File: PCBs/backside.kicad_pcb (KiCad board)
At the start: 2 copper layers, 147.3 x 110.5 mm, 66 parts, among them J1 9Pin, J14 Conn_01x07_Male, J15 Conn_01x07_Male, J16 Conn_01x07_Male, J17 Conn_01x04_Male, J18 Conn_02x17_Odd_Even, J3 Power, J4 Conn_01x17_Male, J5 Matrix, J6 Conn_01x17_Male, J7 Driver output 2, J8 Conn_01x04_Male, J9 Conn_01x30_Male, U1 HT1632C-52LQFP, U2 HT1632C-52LQFP, U3 STM32F103C8T6

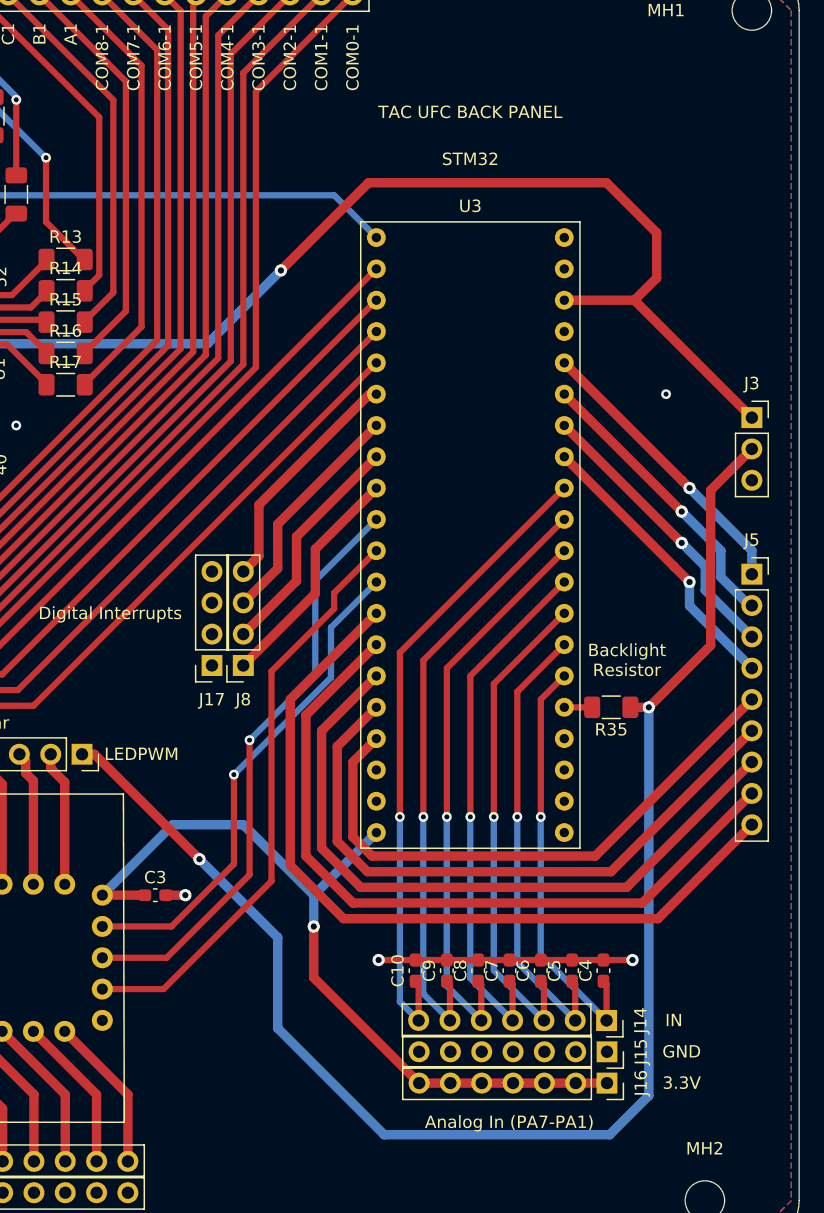
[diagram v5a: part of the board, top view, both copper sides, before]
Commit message: Fixed design error
Untested as of now.
Removed direct connection from PWM out to LEDs, as the PWM pins on the bluepill can't provide enough current. Added P channel mosfet, and individual resistors per parallel LED. For now, the single resistor for all LEDs is still present, but bypassable via jumper, for the sake of backwards compatibility.
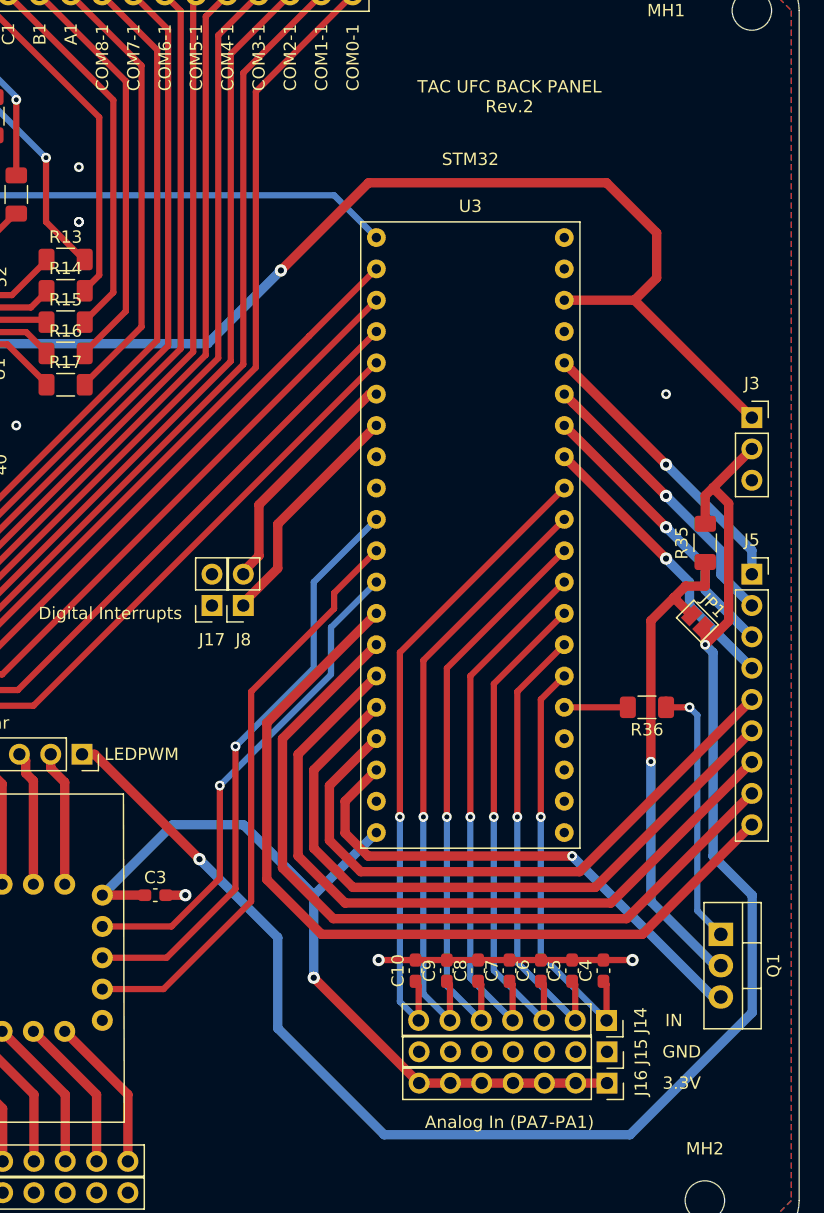
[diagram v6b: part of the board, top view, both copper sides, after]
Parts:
- added JP1: R35 Bypass, Jumper:SolderJumper-2_P1.3mm_Open_Pad1.0x1.5mm, F.Cu at (120.7, 101.6)
- added Q1: IPP120P04P4L03, Package_TO_SOT_THT:TO-220-3_Vertical, F.Cu at (122.6, 127.0)
- added R36: 100R, Resistor_SMD:R_1206_3216Metric_Pad1.30x1.75mm_HandSolder, F.Cu at (116.6, 108.6)
- J17, J8: value Conn_01x04_Male -> Conn_01x02_Male; footprint Connector_PinSocket_2.54mm:PinSocket_1x04_P2.54mm_Vertical -> Connector_PinSocket_2.54mm:PinSocket_1x02_P2.54mm_Vertical
- R35: value 100R -> 20R
- moved R35 15.4 mm to (121.3, 95.2), turned to 270 degrees
- moved J17 4.86 mm to (81.3, 100.3)
- moved J8 4.86 mm to (83.8, 100.3)
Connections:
- R35 pad 2: Net-(R35-Pad2) -> Net-(JP1-Pad1)
- U3 pad 10: Net-(R35-Pad2) -> Net-(R36-Pad2)
- U3 pad 30: /DigInt4 -> /DigInt2
- U3 pad 31: /DigInt3 -> /DigInt1
- U3 pad 32: /DigInt2 -> Net-(U3-Pad32)
- U3 pad 33: /DigInt1 -> Net-(U3-Pad33)
- U3 pad 50: Net-(U3-Pad50) -> /5V
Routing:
- net /5V: track 0.00 -> 42.2 mm, vias 0 -> 1
- net Net-(JP1-Pad1): track 0.00 -> 40.2 mm, vias 0 -> 1
- net Net-(Q1-Pad1): track 0.00 -> 22.0 mm, vias 0 -> 1
- net /DigInt4: track 19.2 -> 0.00 mm
- net /DigInt3: track 18.9 -> 0.00 mm
- net /LEDPWM: track 121.9 -> 130.2 mm
- net Net-(R36-Pad2): track 0.00 -> 5.16 mm
- net /ROW4: track 65.7 -> 70.1 mm
- net /ROW3: track 60.9 -> 65.2 mm
- net /ROW2: track 56.2 -> 60.4 mm
- net /ROW1: track 51.6 -> 55.6 mm
- net /ROW0: track 47.0 -> 50.9 mm
- net Net-(R35-Pad2): track 2.35 -> 0.00 mm
- net /GND: vias 15 -> 18
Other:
- board text added: "TAC UFC BACK PANEL Rev.2"
- board text removed: "Backlight Resistor"
- board text removed: "TAC UFC BACK PANEL"

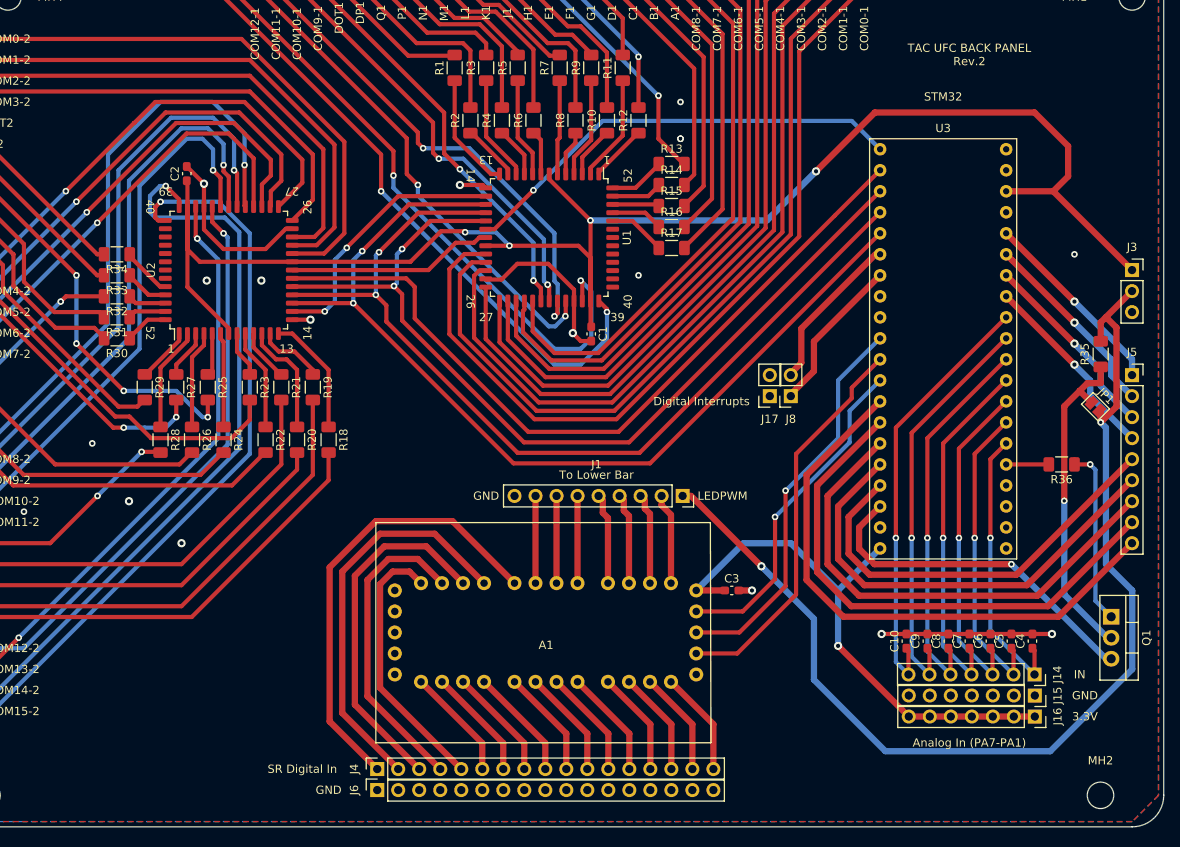
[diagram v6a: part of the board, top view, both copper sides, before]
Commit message: Major revision to backside PCB
Re-arranged pin assignments on the bluepill; sacrificed 4 Analog inputs for 2 more digital interrupts, and 2 more SPI CS pins.
Added two RJ12 connectors so that the board can be connected to other devices that use just shift registers, such as MFDs
Replaced footprint for 3x shift register sub-assembly PCB with 2 DIP16 74hc165s, and pullups and bypass caps.
Re-arranged and replaced 0.1" headers as appropriate.
Removed R35 and its bypass jumper, connecting LEDPWM directly to the MOSFET drain.
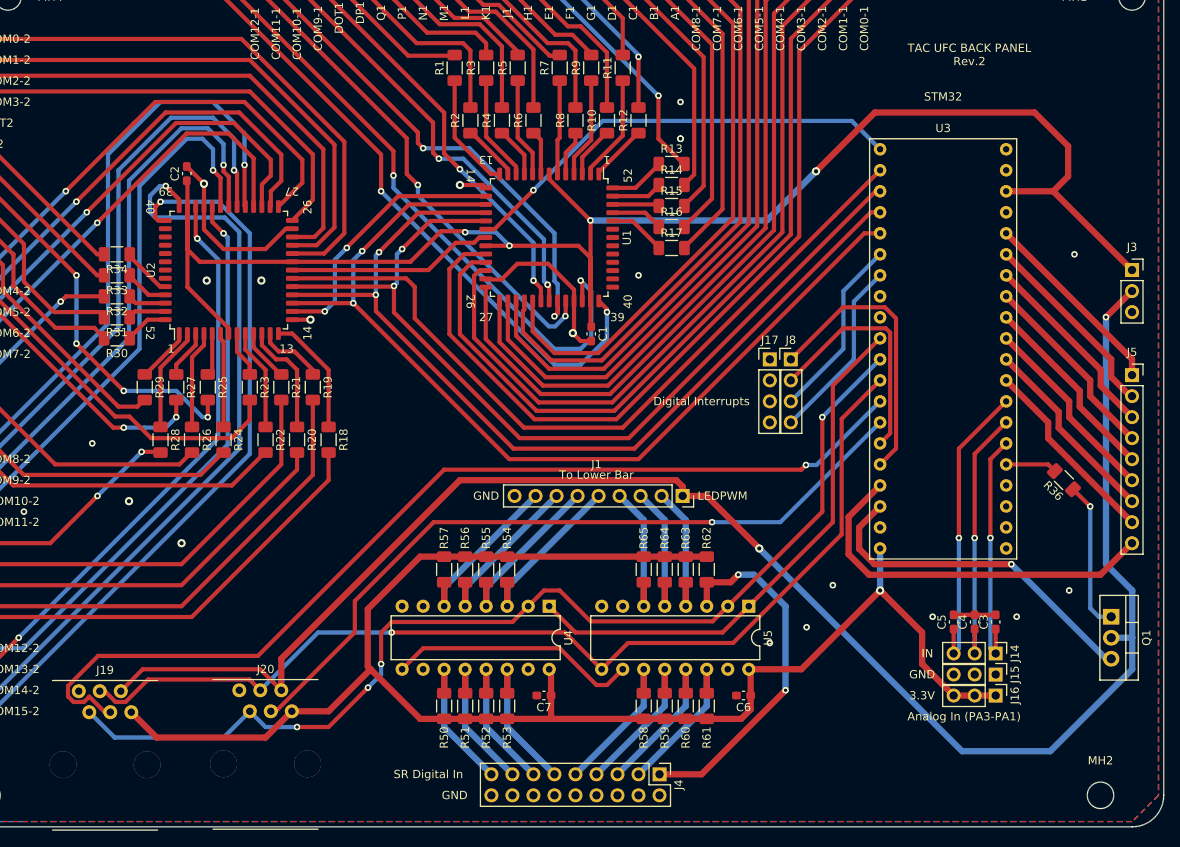
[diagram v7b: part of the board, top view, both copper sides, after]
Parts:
- removed A1: ShiftRegisterBoard, UFC:ShiftRegisterBoardPins
- removed C10, C8, C9: .1uF, Capacitor_SMD:C_0603_1608Metric_Pad1.08x0.95mm_HandSolder
- removed J6: Conn_01x17_Male, Connector_PinSocket_2.54mm:PinSocket_1x17_P2.54mm_Vertical
- removed JP1: R35 Bypass, Jumper:SolderJumper-2_P1.3mm_Open_Pad1.0x1.5mm
- removed R35: 20R, Resistor_SMD:R_1206_3216Metric_Pad1.30x1.75mm_HandSolder
- added J19: RJ12, UFC:SS-6466-NF, F.Cu at (0.91, 136.0)
- added J20: RJ12, UFC:SS-6466-NF, F.Cu at (20.3, 135.9)
- added R50: 10K, Resistor_SMD:R_1206_3216Metric_Pad1.30x1.75mm_HandSolder, F.Cu at (41.9, 137.8)
- added R51: 10K, Resistor_SMD:R_1206_3216Metric_Pad1.30x1.75mm_HandSolder, F.Cu at (44.5, 137.8)
- added R52: 10K, Resistor_SMD:R_1206_3216Metric_Pad1.30x1.75mm_HandSolder, F.Cu at (47.0, 137.8)
- added R53: 10K, Resistor_SMD:R_1206_3216Metric_Pad1.30x1.75mm_HandSolder, F.Cu at (49.5, 137.8)
- added R54: 10K, Resistor_SMD:R_1206_3216Metric_Pad1.30x1.75mm_HandSolder, F.Cu at (49.5, 121.3)
- added R55: 10K, Resistor_SMD:R_1206_3216Metric_Pad1.30x1.75mm_HandSolder, F.Cu at (47.0, 121.3)
- added R56: 10K, Resistor_SMD:R_1206_3216Metric_Pad1.30x1.75mm_HandSolder, F.Cu at (44.5, 121.3)
- added R57: 10K, Resistor_SMD:R_1206_3216Metric_Pad1.30x1.75mm_HandSolder, F.Cu at (41.9, 121.3)
- added R58: 10K, Resistor_SMD:R_1206_3216Metric_Pad1.30x1.75mm_HandSolder, F.Cu at (66.0, 137.8)
- added R59: 10K, Resistor_SMD:R_1206_3216Metric_Pad1.30x1.75mm_HandSolder, F.Cu at (68.6, 137.8)
- added R60: 10K, Resistor_SMD:R_1206_3216Metric_Pad1.30x1.75mm_HandSolder, F.Cu at (71.1, 137.8)
- added R61: 10K, Resistor_SMD:R_1206_3216Metric_Pad1.30x1.75mm_HandSolder, F.Cu at (73.7, 137.8)
- added R62: 10K, Resistor_SMD:R_1206_3216Metric_Pad1.30x1.75mm_HandSolder, F.Cu at (73.7, 121.3)
- added R63: 10K, Resistor_SMD:R_1206_3216Metric_Pad1.30x1.75mm_HandSolder, F.Cu at (71.1, 121.3)
- added R64: 10K, Resistor_SMD:R_1206_3216Metric_Pad1.30x1.75mm_HandSolder, F.Cu at (68.6, 121.3)
- added R65: 10K, Resistor_SMD:R_1206_3216Metric_Pad1.30x1.75mm_HandSolder, F.Cu at (66.0, 121.3)
- added U4: 74HC165, Package_DIP:DIP-16_W7.62mm, F.Cu at (54.6, 125.7)
- added U5: 74HC165, Package_DIP:DIP-16_W7.62mm, F.Cu at (78.7, 125.7)
- J14, J15, J16: value Conn_01x07_Male -> Conn_01x03_Male; footprint Connector_PinSocket_2.54mm:PinSocket_1x07_P2.54mm_Vertical -> Connector_PinHeader_2.54mm:PinHeader_1x03_P2.54mm_Vertical
- J17, J8: value Conn_01x02_Male -> Conn_01x04_Male; footprint Connector_PinSocket_2.54mm:PinSocket_1x02_P2.54mm_Vertical -> Connector_PinHeader_2.54mm:PinHeader_1x04_P2.54mm_Vertical
- J4: value Conn_01x17_Male -> Conn_02x09_Odd_Even; footprint Connector_PinSocket_2.54mm:PinSocket_1x17_P2.54mm_Vertical -> Connector_PinHeader_2.54mm:PinHeader_2x09_P2.54mm_Vertical
- moved C7 51.9 mm to (54.0, 136.5), turned to 180 degrees
- moved J4 34.1 mm to (67.9, 146.1), turned to 270 degrees
- moved C3 32.1 mm to (108.6, 127.6), turned to 90 degrees
- moved C6 30.6 mm to (78.1, 136.5), turned to 180 degrees
- moved C4 7.36 mm to (106.0, 127.6)
- moved C5 7.36 mm to (103.5, 127.6)
- moved J15 5.37 mm to (108.6, 134.0)
- moved J16 5.37 mm to (108.6, 136.5)
- moved J14 5.34 mm to (108.6, 131.4)
- moved J17 4.44 mm to (81.3, 95.9), turned to 0 degrees
- moved J8 4.44 mm to (83.8, 95.9), turned to 0 degrees
- moved R36 1.93 mm to (116.8, 110.5), turned to 135 degrees
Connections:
- C3 pad 1: /3.3V -> /Analog1
- C4 pad 1: /Analog1 -> /Analog2
- C5 pad 1: /Analog2 -> /Analog3
- C6 pad 1: /Analog3 -> /3.3V
- C7 pad 1: /Analog4 -> /3.3V
- J4 pad 1: /DIN17 -> /DIN1
- J4 pad 10: /DIN5 -> /GND
- J4 pad 12: /DIN7 -> /GND
- J4 pad 13: /DIN8 -> /DIN7
- J4 pad 14: /DIN9 -> /GND
- J4 pad 15: /DIN10 -> /DIN8
- J4 pad 16: /DIN11 -> /GND
- J4 pad 17: /DIN12 -> /DIN9
- J4 pad 2: /DIN16 -> /GND
- J4 pad 3: /DIN15 -> /DIN2
- J4 pad 4: /DIN14 -> /GND
- J4 pad 5: /DIN13 -> /DIN3
- J4 pad 6: /DIN1 -> /GND
- J4 pad 7: /DIN2 -> /DIN4
- J4 pad 8: /DIN3 -> /GND
- J4 pad 9: /DIN4 -> /DIN5
- Q1 pad 2: Net-(JP1-Pad1) -> /LEDPWM
- U3 pad 14: /Analog4 -> /ROW3
- U3 pad 15: /Analog5 -> /ROW2
- U3 pad 16: /Analog6 -> /ROW1
- U3 pad 17: /Analog7 -> /ROW0
- U3 pad 30: /DigInt2 -> /DigInt3
- U3 pad 31: /DigInt1 -> /DigInt4
- U3 pad 41: /ROW4 -> /SRCS2
- U3 pad 42: /ROW3 -> /SRCS3
- U3 pad 43: /ROW2 -> /DigInt2
- U3 pad 45: /ROW1 -> /DigInt1
- U3 pad 46: /ROW0 -> /ROW4
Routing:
- net /3.3V: track 263.4 -> 387.8 mm
- net /SRCS2: track 0.00 -> 120.1 mm, vias 0 -> 1
- net /SRCS3: track 0.00 -> 90.3 mm, vias 0 -> 1
- net /SRMISO: track 40.4 -> 123.9 mm
- net /SRCLK: track 47.7 -> 130.2 mm, vias 0 -> 4
- net /LEDPWM: track 130.2 -> 206.4 mm
- net /DIN17: track 54.5 -> 0.00 mm
- net /Analog7: track 52.6 -> 0.00 mm, vias 1 -> 0
- net /Analog6: track 49.5 -> 0.00 mm, vias 1 -> 0
- net /DIN16: track 48.2 -> 0.00 mm
- net /Analog5: track 46.5 -> 0.00 mm, vias 1 -> 0
- net /Analog4: track 43.4 -> 0.00 mm, vias 1 -> 0
- net /DIN15: track 43.0 -> 0.00 mm
- net /ROW3: track 65.2 -> 23.4 mm
- net Net-(JP1-Pad1): track 40.2 -> 0.00 mm, vias 1 -> 0
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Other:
- board text added: "Analog In (PA3-PA1)"
- board text removed: "Analog In (PA7-PA1)"

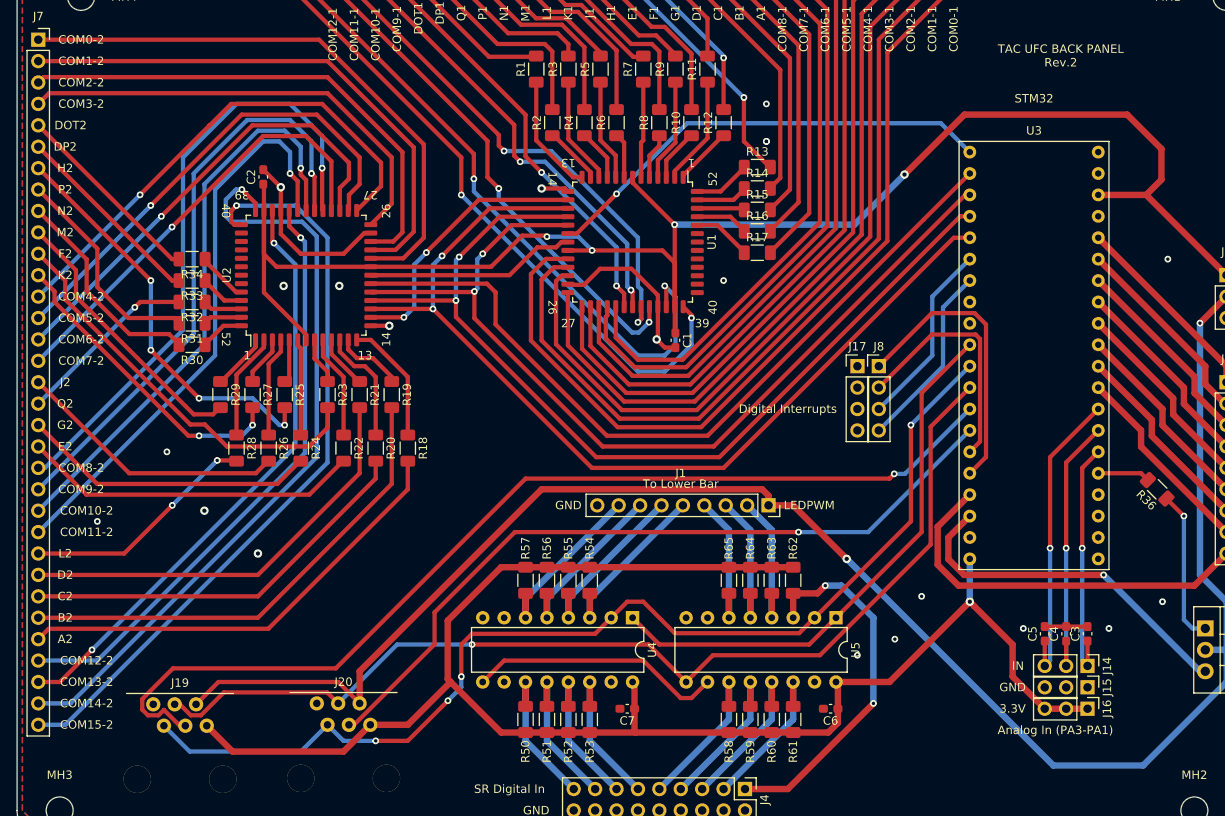
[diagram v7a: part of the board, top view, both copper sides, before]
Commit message: Corrected extra shift register pins
Replaced two latch pins with one latch and one data to one port, and made the other port daisy chained after the two shift registers on the board
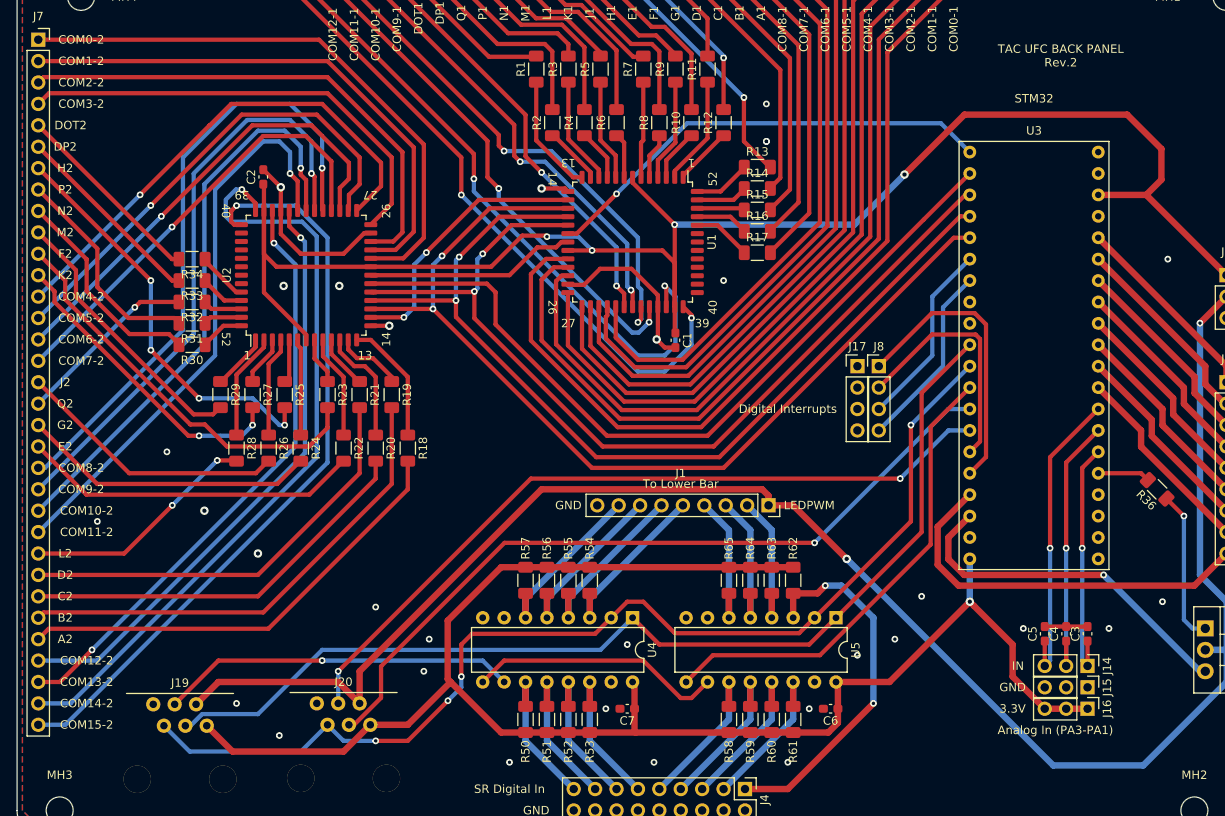
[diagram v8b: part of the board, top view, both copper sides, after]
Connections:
- J19 pad 3: /SRMISO -> /DSIN
- J19 pad 4: /SRCS2 -> /SRCS
- J20 pad 3: /SRMISO -> /SRMISO2
- J20 pad 4: /SRCS3 -> /SRCS2
- U3 pad 42: /SRCS3 -> /SRMISO2
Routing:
- net /SRMISO2: track 0.00 -> 90.6 mm, vias 0 -> 2
- net /SRCS3: track 90.3 -> 0.00 mm, vias 1 -> 0
- net /SRMISO: track 123.9 -> 56.3 mm, vias 1 -> 0
- net /SRCS: track 65.7 -> 124.1 mm
- net /DSIN: track 0.00 -> 42.3 mm, vias 0 -> 1
- net /SRCS2: track 120.1 -> 91.4 mm
- net /GND: vias 21 -> 32
